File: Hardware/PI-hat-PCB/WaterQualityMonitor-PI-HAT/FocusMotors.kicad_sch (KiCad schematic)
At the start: 4 parts

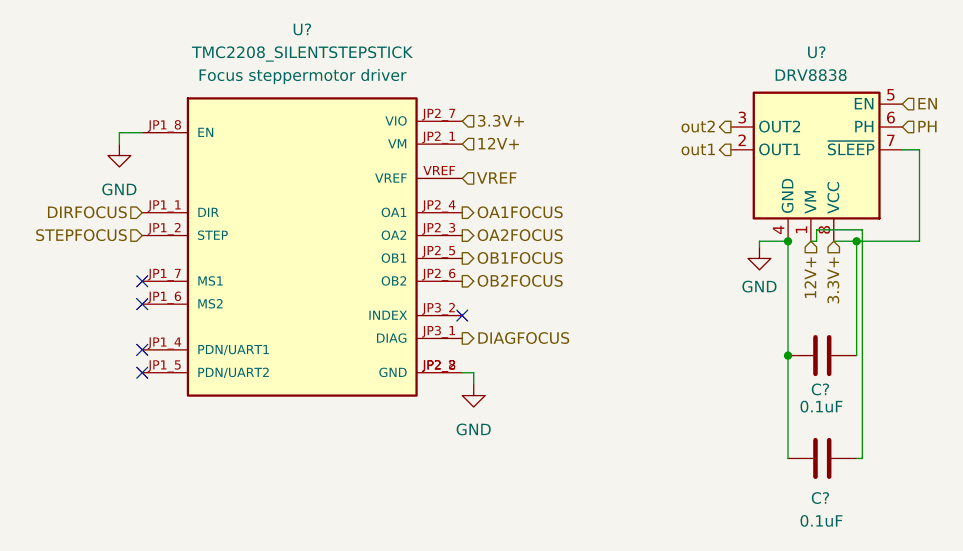
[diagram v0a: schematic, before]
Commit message: assigent footprints to all current components
I chose 1206smd handsolderable for caps and resistors and inductors, may need to be revised
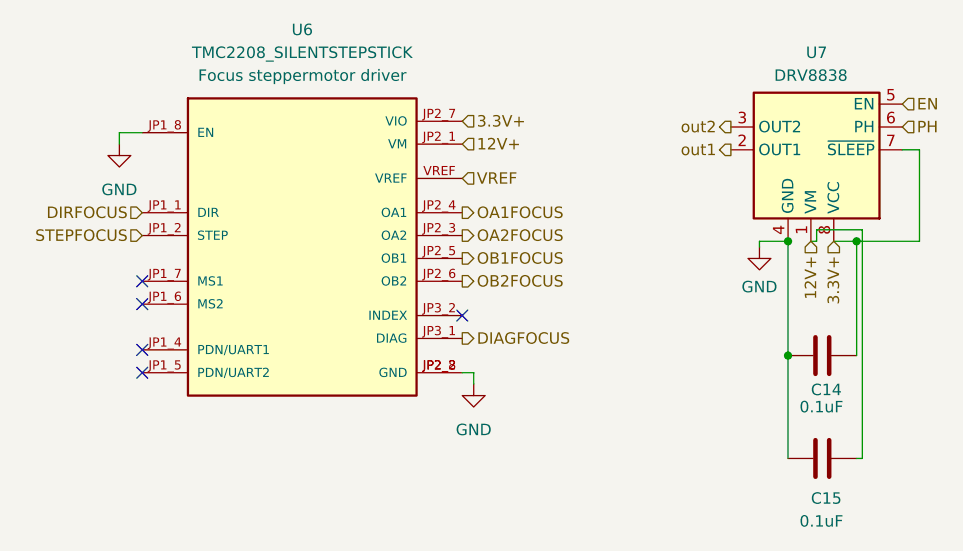
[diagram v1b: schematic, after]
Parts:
- C14, C15: renamed from C?; footprint (none) -> Capacitor_SMD:C_1206_3216Metric_Pad1.33x1.80mm_HandSolder
- U6: renamed from U?; footprint MODULE_TMC2208_SILENTSTEPSTICK -> Footprints:TMC2208_SILENTSTEPSTICK
- gave numbers to parts that had none: 1
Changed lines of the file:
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@@
   (symbol (lib_name "TMC2208_SILENTSTEPSTICK_1") (lib_id "TMC2208_SILENTSTEPSTICK:TMC2208_SILENTSTEPSTICK") (at 123.825 100.33 0) (unit 1)
     (in_bom yes) (on_board yes) (fields_autoplaced)
-    (property "Reference" "U?" (id 0) (at 123.825 74.93 0))
+    (property "Reference" "U6" (id 0) (at 123.825 74.93 0))
     (property "Value" "TMC2208_SILENTSTEPSTICK" (id 1) (at 123.825 77.47 0))
-    (property "Footprint" "MODULE_TMC2208_SILENTSTEPSTICK" (id 2) (at 108.585 119.38 0)
+    (property "Footprint" "Footprints:TMC2208_SILENTSTEPSTICK" (id 2) (at 108.585 119.38 0)
       (effects (font (size 1.27 1.27)) (justify left bottom) hide)
     )
@@
   (symbol (lib_id "Device:C") (at 181.61 122.555 90) (unit 1)
     (in_bom yes) (on_board yes)
-    (property "Reference" "C?" (id 0) (at 180.34 127 90)
+    (property "Reference" "C15" (id 0) (at 180.34 127 90)
       (effects (font (size 1.27 1.27)) (justify right))
     )
@@
       (effects (font (size 1.27 1.27)) (justify right))
     )
-    (property "Footprint" "" (id 2) (at 185.42 121.5898 0)
+    (property "Footprint" "Capacitor_SMD:C_1206_3216Metric_Pad1.33x1.80mm_HandSolder" (id 2) (at 185.42 121.5898 0)
       (effects (font (size 1.27 1.27)) hide)
     )
@@
   (symbol (lib_id "Driver_Motor:DRV8838") (at 180.34 85.725 180) (unit 1)
     (in_bom yes) (on_board yes)
-    (property "Reference" "U?" (id 0) (at 180.975 77.47 0))
+    (property "Reference" "U7" (id 0) (at 180.975 77.47 0))
     (property "Value" "DRV8838" (id 1) (at 180.34 80.01 0))
     (property "Footprint" "Package_SON:WSON-8-1EP_2x2mm_P0.5mm_EP0.9x1.6mm" (id 2) (at 201.93 85.725 0)
@@
   (symbol (lib_id "Device:C") (at 181.61 111.125 90) (unit 1)
     (in_bom yes) (on_board yes)
-    (property "Reference" "C?" (id 0) (at 180.34 114.935 90)
+    (property "Reference" "C14" (id 0) (at 180.34 114.935 90)
       (effects (font (size 1.27 1.27)) (justify right))
     )
@@
       (effects (font (size 1.27 1.27)) (justify right))
     )
-    (property "Footprint" "" (id 2) (at 185.42 110.1598 0)
+    (property "Footprint" "Capacitor_SMD:C_1206_3216Metric_Pad1.33x1.80mm_HandSolder" (id 2) (at 185.42 110.1598 0)
       (effects (font (size 1.27 1.27)) hide)
     )
